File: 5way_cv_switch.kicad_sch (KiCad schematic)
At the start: 16 parts, among them J1 I/O connector, J2 5-way Switch Connector, U1 HT7550-1, U2 opamp_dbv2

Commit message: minor updates
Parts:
- added H5: MountingHole, cycfi_library:hole_2.65mm, symbol Mechanical:MountingHole
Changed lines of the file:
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@@
     (pin "1")
+  )
+  (symbol (lib_id "Mechanical:MountingHole") (at 233.68 68.58 0) (unit 1)
+    (in_bom yes) (on_board yes) (fields_autoplaced)
+    (property "Reference" "H5" (id 0) (at 236.22 67.7453 0)
+      (effects (font (size 1.27 1.27)) (justify left))
+    )
+    (property "Value" "MountingHole" (id 1) (at 236.22 70.2822 0)
+      (effects (font (size 1.27 1.27)) (justify left))
+    )
+    (property "Footprint" "cycfi_library:hole_2.65mm" (id 2) (at 233.68 68.58 0)
+      (effects (font (size 1.27 1.27)) hide)
+    )
+    (property "Datasheet" "~" (id 3) (at 233.68 68.58 0)
+      (effects (font (size 1.27 1.27)) hide)
+    )
   )
   (symbol (lib_id "power:PWR_FLAG") (at 111.76 66.04 180) (unit 1)
@@
       (reference "H4") (unit 1) (value "single_pad") (footprint "cycfi_library:cond_hole_rect_1.2x3.5mm")
     )
+    (path "/460147d8-e4b6-4910-88e9-07d1ddd6c2df"
+      (reference "H5") (unit 1) (value "MountingHole") (footprint "cycfi_library:hole_2.65mm")
+    )
     (path "/cd61a421-8b7f-4ccf-a635-570d47a12576"

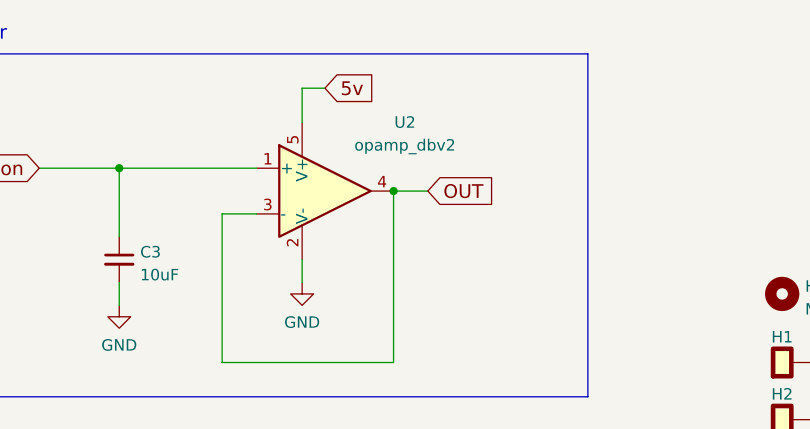
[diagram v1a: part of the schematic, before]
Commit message: Added small CV Pot
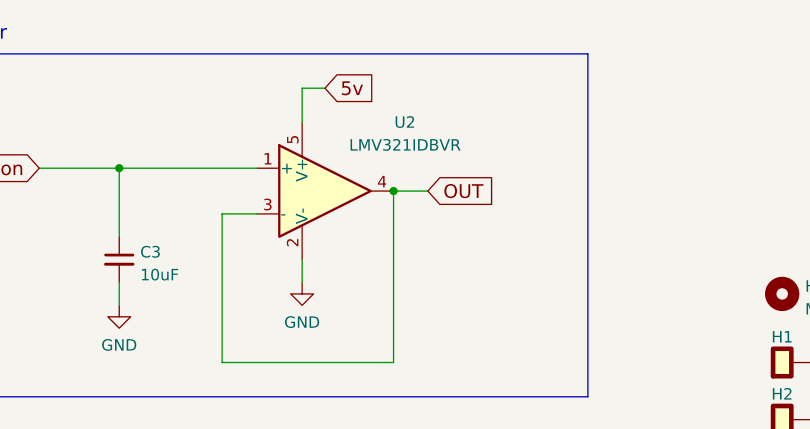
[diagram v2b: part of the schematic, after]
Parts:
- U2: value opamp_dbv2 -> LMV321IDBVR
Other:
- title: 5-way CV Module -> 5-way CV Switch
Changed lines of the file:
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@@
   (paper "A4")
   (title_block
-    (title "5-way CV Module")
+    (title "5-way CV Switch")
     (date "2022-02-24")
     (rev "v3.0")
@@
     (in_bom yes) (on_board yes)
     (property "Reference" "U2" (id 0) (at 191.77 49.53 0))
-    (property "Value" "opamp_dbv2" (id 1) (at 191.77 52.0669 0))
+    (property "Value" "LMV321IDBVR" (id 1) (at 191.77 52.0669 0))
     (property "Footprint" "Package_TO_SOT_SMD:SOT-23-5" (id 2) (at 180.34 62.23 0)
       (effects (font (size 1.27 1.27)) (justify left) hide)
@@
     )
     (path "/e69c64f9-717d-4a97-b3df-80325ec2fa63"
-      (reference "U2") (unit 1) (value "opamp_dbv2") (footprint "Package_TO_SOT_SMD:SOT-23-5")
-    )
-  )
+      (reference "U2") (unit 1) (value "LMV321IDBVR") (footprint "Package_TO_SOT_SMD:SOT-23-5")
+    )
+  )

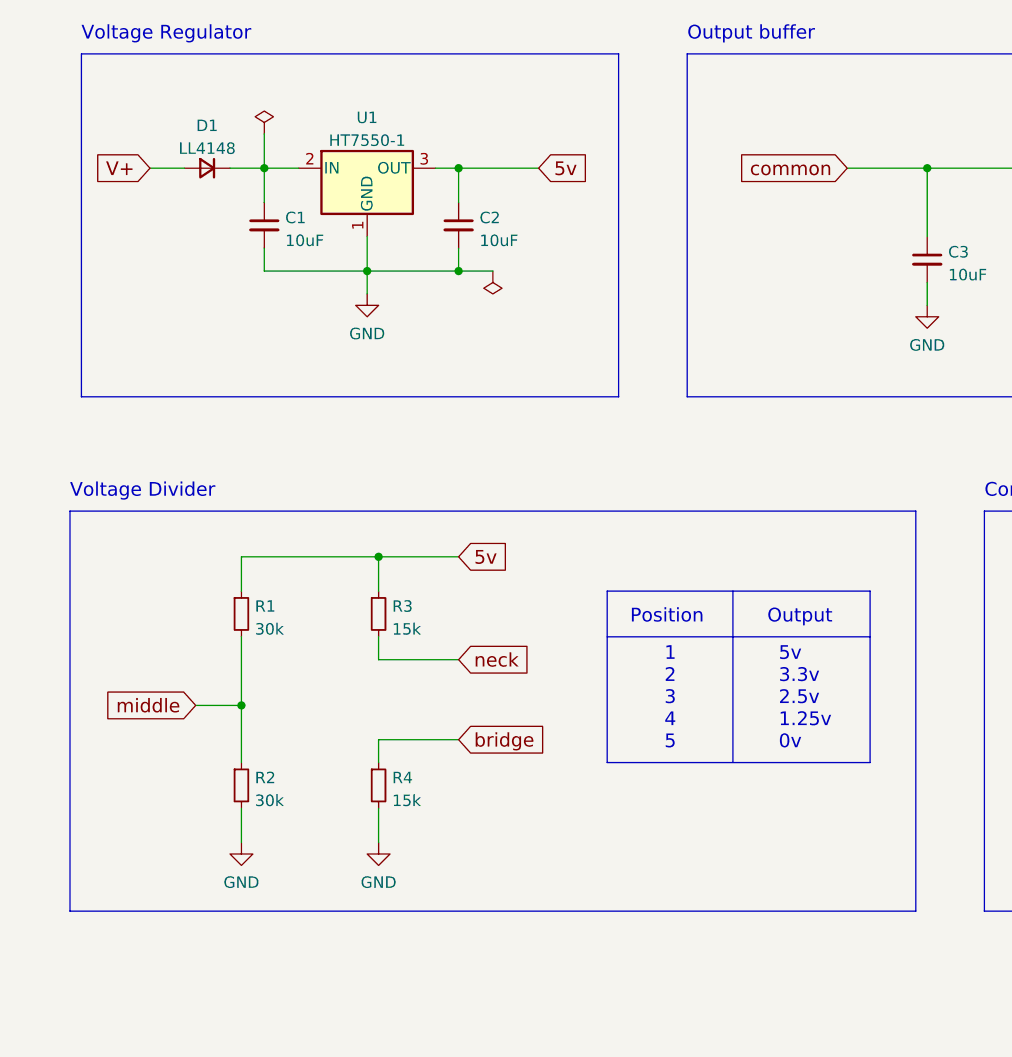
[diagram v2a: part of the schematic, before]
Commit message: Updated components for JLCPCB PCBA
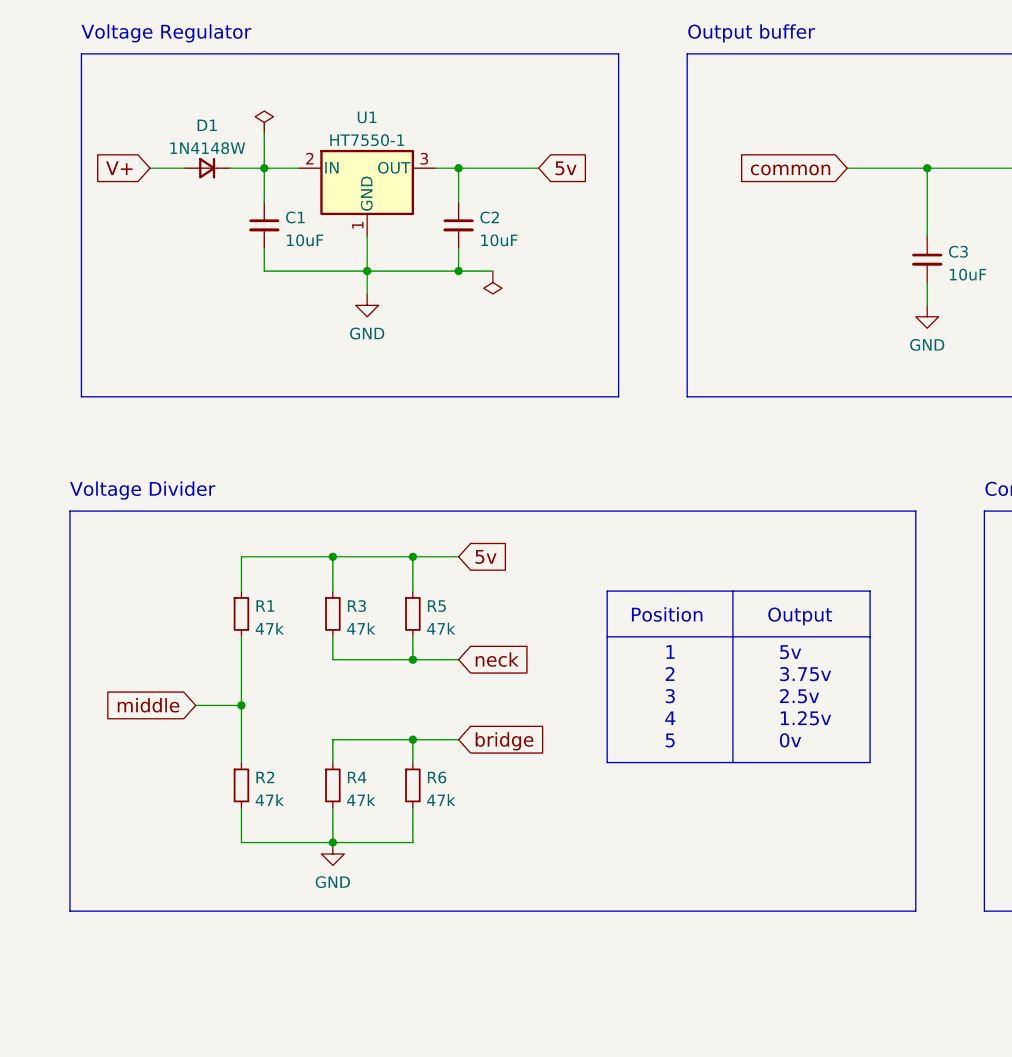
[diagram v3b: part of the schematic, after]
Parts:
- added R5, R6: 47k, Resistor_SMD:R_0402_1005Metric, symbol Device:R_Small
- C1, C2, C3: footprint Capacitor_SMD:C_0603_1608Metric -> Capacitor_SMD:C_0805_2012Metric; LCSC (none) -> C15850
- D1: value LL4148 -> 1N4148W; footprint Diode_SMD:D_MiniMELF -> Diode_SMD:D_SOD-123; LCSC (none) -> C81598
- R1, R2: value 30k -> 47k; footprint Resistor_SMD:R_0603_1608Metric -> Resistor_SMD:R_0402_1005Metric; LCSC (none) -> C25792
- R3, R4: value 15k -> 47k; footprint Resistor_SMD:R_0603_1608Metric -> Resistor_SMD:R_0402_1005Metric; LCSC (none) -> C25792
- U1: LCSC (none) -> C16106
- U2: LCSC (none) -> C7972
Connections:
- net 5v: now also R5.1
- net GND: now also R6.2
- net bridge: now also R6.1
- net neck: now also R5.2
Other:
- note added: "5v 3.75v 2.5v 1.25v 0v"
- note removed: "5v 3.3v 2.5v 1.25v 0v"

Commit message: Updates: - Fixed overlapping fill regions when paneling - Added JLCPCB rotation
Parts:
- U1: JLCPCB_CORRECTION (none) -> 0;0;180
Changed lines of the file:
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@@
+      (effects (font (size 1.524 1.524)) hide)
+    )
+    (property "JLCPCB_CORRECTION" "0;0;180" (id 5) (at 97.79 54.61 0)
       (effects (font (size 1.524 1.524)) hide)
     )
